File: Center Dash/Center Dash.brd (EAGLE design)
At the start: 159 x 86.7 mm, 73 parts, among them J1 502585-0470, U1 ADG3304BRUZ-REEL7, U2 TPS54540DDARQ1

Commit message: Worked on code
Updated board layouts since shit changed
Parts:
- added Q1, Q2, Q3, Q4: BSS138, FormE:BSS138
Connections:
- new net AMS_OUT: Q1.D, U$1.P$20
- new net BSPD_OUT: Q3.D, U$1.P$22
- new net IMD_OUT: Q2.D, U$1.P$21
- new net TPS_OUT: Q4.D, U$1.P$23
- net AMS: now also Q1.G; no longer U$1.P$20
- net BSPD: now also Q3.G; no longer U$1.P$22
- net GND: now also Q1.S, Q2.S, Q3.S, Q4.S
- net IMD: now also Q2.G; no longer U$1.P$21
- net TPS: now also Q4.G; no longer U$1.P$23
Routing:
- net AMS: track 40.5 -> 35.2 mm, vias 1 -> 2
- net TPS: track 35.7 -> 30.9 mm, vias 2 -> 3
- net IMD: track 35.5 -> 30.6 mm, vias 2 -> 3
- net BSPD: track 29.4 -> 24.6 mm, vias 0 -> 1
- net TPS_OUT: track 0.00 -> 2.93 mm
- net IMD_OUT: track 0.00 -> 2.83 mm
- net AMS_OUT: track 0.00 -> 2.80 mm
- net BSPD_OUT: track 0.00 -> 2.77 mm
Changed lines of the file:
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@@
 <attribute name="VALUE" x="19.812" y="24.511" size="1.27" layer="27"/>
+</element>
+<element name="Q1" library="FormE" package="BSS138" value="BSS138" x="1.905" y="61.976" smashed="yes" rot="MR0">
+<attribute name="NAME" x="4.445" y="59.436" size="1.27" layer="26" rot="MR90"/>
+</element>
+<element name="Q2" library="FormE" package="BSS138" value="BSS138" x="5.842" y="61.976" smashed="yes" rot="MR0">
+<attribute name="NAME" x="8.382" y="59.436" size="1.27" layer="26" rot="MR90"/>
+</element>
+<element name="Q3" library="FormE" package="BSS138" value="BSS138" x="10.033" y="61.976" smashed="yes" rot="MR0">
+<attribute name="NAME" x="12.573" y="59.436" size="1.27" layer="26" rot="MR90"/>
+</element>
+<element name="Q4" library="FormE" package="BSS138" value="BSS138" x="14.097" y="61.849" smashed="yes" rot="MR0">
+<attribute name="NAME" x="16.637" y="59.309" size="1.27" layer="26" rot="MR90"/>
 </element>
 </elements>
@@
 <wire x1="-30.876" y1="69.536" x2="-33.701" y2="69.536" width="0.3048" layer="16"/>
 <wire x1="-33.701" y1="69.536" x2="-33.906" y2="69.331" width="0.3048" layer="16"/>
+<contactref element="Q4" pad="S"/>
+<contactref element="Q3" pad="S"/>
+<contactref element="Q2" pad="S"/>
+<contactref element="Q1" pad="S"/>
 </signal>
 <signal name="+15V">
@@
 <signal name="AMS">
 <contactref element="U$2" pad="5"/>
-<contactref element="U$1" pad="P$20"/>
-<wire x1="2" y1="65.937" x2="2" y2="54.769" width="0.3048" layer="1"/>
-<wire x1="2" y1="54.769" x2="2.54" y2="54.229" width="0.3048" layer="1"/>
-<wire x1="2.54" y1="54.229" x2="2.54" y2="39.116" width="0.3048" layer="1"/>
+<wire x1="2.54" y1="39.116" x2="2.54" y2="54.229" width="0.3048" layer="1"/>
 <wire x1="2.54" y1="39.116" x2="2.921" y2="38.735" width="0.3048" layer="1"/>
 <via x="2.921" y="38.735" extent="1-16" drill="0.35"/>
@@
 <wire x1="14.224" y1="38.354" x2="14.224" y2="37.131" width="0.3048" layer="16"/>
 <wire x1="14.224" y1="37.131" x2="14.089" y2="36.996" width="0.3048" layer="16"/>
+<contactref element="Q1" pad="G"/>
+<wire x1="2.54" y1="54.229" x2="2.855" y2="54.544" width="0.3048" layer="1"/>
+<wire x1="2.855" y1="54.544" x2="2.855" y2="60.776" width="0.3048" layer="1"/>
+<via x="2.855" y="60.776" extent="1-16" drill="0.35"/>
 </signal>
 <signal name="IMD">
 <contactref element="U$2" pad="6"/>
-<contactref element="U$1" pad="P$21"/>
-<wire x1="6" y1="65.937" x2="6" y2="54.387" width="0.3048" layer="1"/>
-<wire x1="6" y1="54.387" x2="5.207" y2="53.594" width="0.3048" layer="1"/>
+<wire x1="6" y1="54.387" x2="5.9055" y2="54.2925" width="0.3048" layer="1"/>
+<wire x1="5.9055" y1="54.2925" x2="5.207" y2="53.594" width="0.3048" layer="1"/>
 <wire x1="5.207" y1="53.594" x2="5.207" y2="39.164" width="0.3048" layer="1"/>
 <wire x1="5.207" y1="39.164" x2="5.334" y2="39.037" width="0.3048" layer="1"/>
@@
 <wire x1="11.43" y1="39.037" x2="11.549" y2="38.918" width="0.3048" layer="1"/>
 <wire x1="11.549" y1="38.918" x2="11.549" y2="36.996" width="0.3048" layer="1"/>
+<contactref element="Q2" pad="G"/>
+<wire x1="6" y1="54.387" x2="6.792" y2="55.179" width="0.3048" layer="1"/>
+<wire x1="6.792" y1="55.179" x2="6.792" y2="60.776" width="0.3048" layer="1"/>
+<via x="6.792" y="60.776" extent="1-16" drill="0.35"/>
 </signal>
 <signal name="BSPD">
 <contactref element="U$2" pad="7"/>
-<contactref element="U$1" pad="P$22"/>
-<wire x1="10" y1="65.937" x2="10" y2="52.7177625" width="0.3048" layer="1"/>
-<wire x1="10" y1="52.7177625" x2="10.0504" y2="52.6673625" width="0.3048" layer="1"/>
-<wire x1="10.0504" y1="52.6673625" x2="10.0504" y2="38.0374" width="0.3048" layer="1"/>
+<wire x1="10.0504" y1="59.8434" x2="10.0504" y2="38.0374" width="0.3048" layer="1"/>
 <wire x1="10.0504" y1="38.0374" x2="9.009" y2="36.996" width="0.3048" layer="1"/>
+<contactref element="Q3" pad="G"/>
+<wire x1="10.0504" y1="59.8434" x2="10.983" y2="60.776" width="0.3048" layer="1"/>
+<via x="10.983" y="60.776" extent="1-16" drill="0.35"/>
 </signal>
 <signal name="TPS">
 <contactref element="U$2" pad="8"/>
-<contactref element="U$1" pad="P$23"/>
-<wire x1="14" y1="65.937" x2="14" y2="53.878" width="0.3048" layer="1"/>
-<wire x1="14" y1="53.878" x2="12.954" y2="52.832" width="0.3048" layer="1"/>
+<wire x1="14" y1="53.878" x2="13.716" y2="53.594" width="0.3048" layer="1"/>
+<wire x1="13.716" y1="53.594" x2="12.954" y2="52.832" width="0.3048" layer="1"/>
 <wire x1="12.954" y1="52.832" x2="12.954" y2="42.291" width="0.3048" layer="1"/>
 <wire x1="12.954" y1="42.291" x2="12.827" y2="42.164" width="0.3048" layer="1"/>
@@
 <wire x1="6.477" y1="42.037" x2="6.469" y2="42.029" width="0.3048" layer="1"/>
 <wire x1="6.469" y1="42.029" x2="6.469" y2="36.996" width="0.3048" layer="1"/>
+<contactref element="Q4" pad="G"/>
+<wire x1="14" y1="53.878" x2="15.047" y2="54.925" width="0.3048" layer="1"/>
+<wire x1="15.047" y1="54.925" x2="15.047" y2="60.649" width="0.3048" layer="1"/>
+<via x="15.047" y="60.649" extent="1-16" drill="0.35"/>
 </signal>
 <signal name="SW_BIT2">
@@
 <wire x1="50.165" y1="57.116" x2="50.165" y2="55.229" width="0.8128" layer="16"/>
 </signal>
+<signal name="AMS_OUT">
+<contactref element="Q1" pad="D"/>
+<contactref element="U$1" pad="P$20"/>
+<wire x1="1.905" y1="63.176" x2="1.905" y2="65.842" width="0.3048" layer="16"/>
+<wire x1="1.905" y1="65.842" x2="2" y2="65.937" width="0.3048" layer="16"/>
+</signal>
+<signal name="IMD_OUT">
+<contactref element="Q2" pad="D"/>
+<contactref element="U$1" pad="P$21"/>
+<wire x1="5.842" y1="63.176" x2="5.842" y2="65.779" width="0.3048" layer="16"/>
+<wire x1="5.842" y1="65.779" x2="6" y2="65.937" width="0.3048" layer="16"/>
+</signal>
+<signal name="BSPD_OUT">
+<contactref element="Q3" pad="D"/>
+<contactref element="U$1" pad="P$22"/>
+<wire x1="10.033" y1="63.176" x2="10.033" y2="65.904" width="0.3048" layer="16"/>
+<wire x1="10.033" y1="65.904" x2="10" y2="65.937" width="0.3048" layer="16"/>
+</signal>
+<signal name="TPS_OUT">
+<contactref element="Q4" pad="D"/>
+<contactref element="U$1" pad="P$23"/>
+<wire x1="14.097" y1="63.049" x2="14.097" y2="65.84" width="0.3048" layer="16"/>
+<wire x1="14.097" y1="65.84" x2="14" y2="65.937" width="0.3048" layer="16"/>
+</signal>
 </signals>

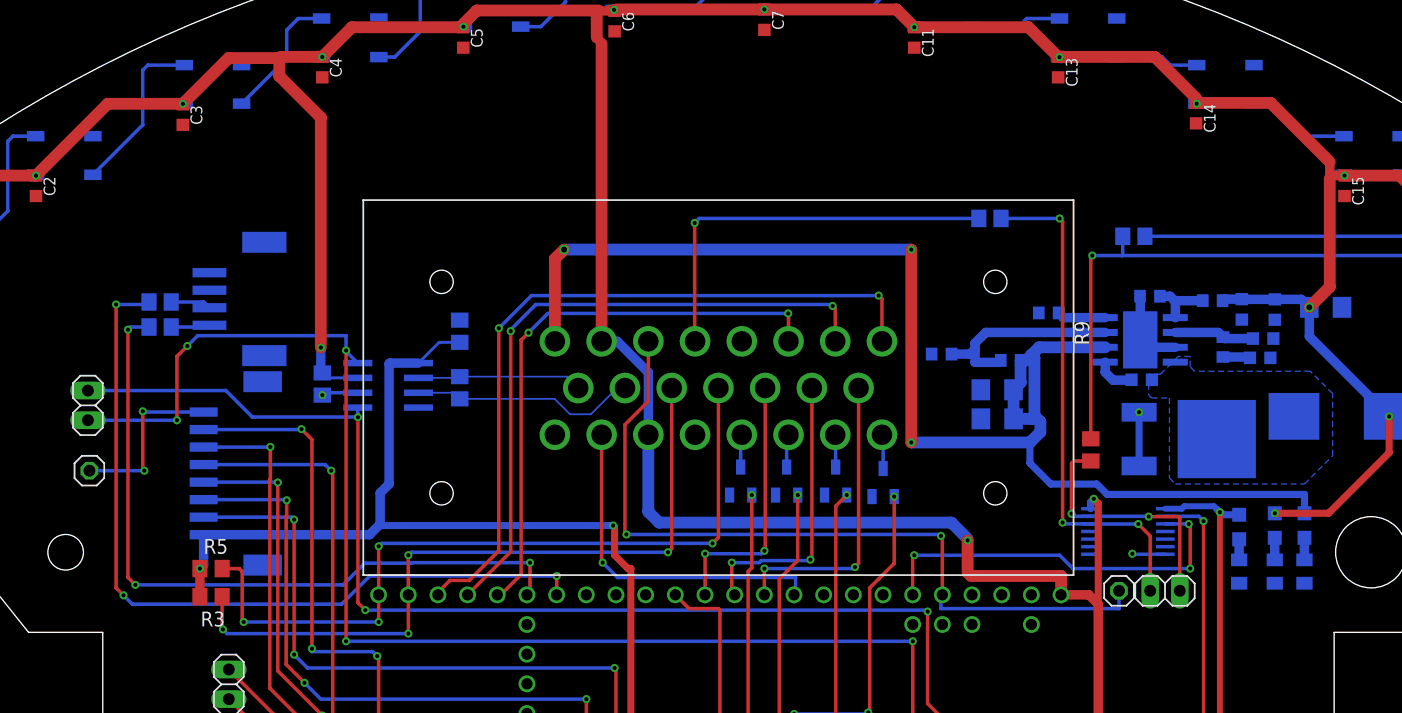
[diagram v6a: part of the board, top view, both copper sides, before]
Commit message: Fix for daqbus CAN
Added another can transceiver for the daq bus
Moved the ignition1 and 2 to different pins to account for the teensy can bus lines
Fixed the can code from flexcan
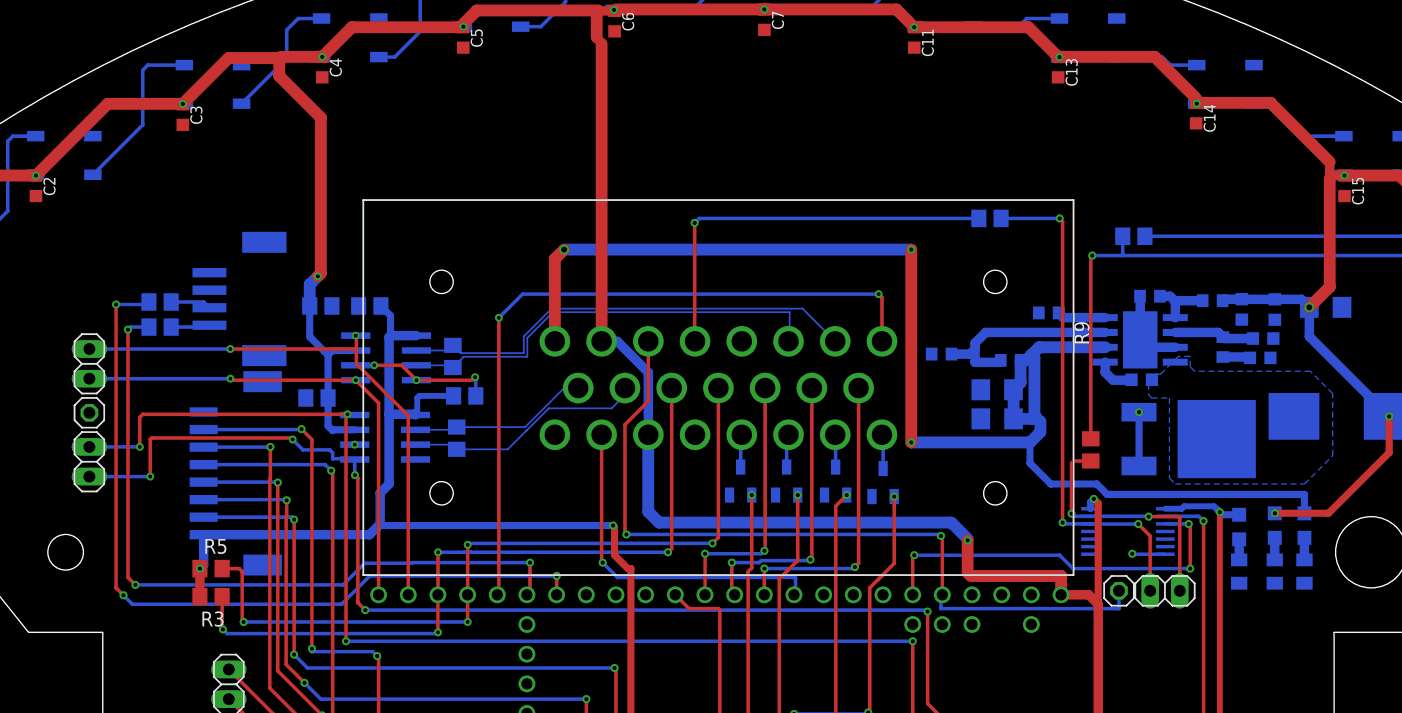
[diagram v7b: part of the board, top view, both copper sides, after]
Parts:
- added C17, C21: .1uF, rcl:C0805
- added JP9: (no value), pinhead:1X02
- added R16: 120, rcl:R0805
- added U4: (no value), FormE:SOIC8-N_MC
- moved C20 5.55 mm to (-21.7, 69.3), turned to 180 degrees
- moved JP4 4.95 mm to (-53.8, 67.8)
- moved JP6 4.83 mm to (-53.8, 63.6), turned to 270 degrees
- moved U3 4.45 mm to (-28.5, 65.7)
- moved R4 4.33 mm to (-22.4, 65.6)
- moved C19 1.28 mm to (-34.4, 69.1), turned to 0 degrees
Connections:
- net CAN_N renamed CARCAN_N
- net CAN_P renamed CARCAN_P
- net CAN_RX renamed CARCAN_RX
- net CAN_TX renamed CARCAN_TX
- removed net SPARE_2: U$1.P$7, U$2.36/A17
- removed net SPARE_3: U$1.P$6, U$2.37/A18
- new net DAQCAN_N: R16.2, U$1.P$7, U4.6
- new net DAQCAN_P: R16.1, U$1.P$6, U4.7
- new net DAQCAN_RX: JP9.2, U$2.34/A15, U4.4
- new net DAQCAN_TX: JP9.1, U$2.33/A14, U4.1
- net +3V3: now also C21.1, U4.5
- net +5V: now also C17.1, U4.3
- net GND: now also C17.2, C21.2, U4.2, U4.8
- net IGNITION_1: now also R3.2, U$1.P$11, U$2.35/A16; no longer R5.2, U$1.P$12, U$2.33/A14
- net IGNITION_2: now also R5.2, U$1.P$12, U$2.36/A17; no longer R3.2, U$1.P$11, U$2.34/A15
- net SPARE_1: now also U$2.37/A18; no longer U$2.35/A16
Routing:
- net SPARE_2: track 55.8 -> 0.00 mm, vias 2 -> 0
- net SPARE_3: track 49.0 -> 0.00 mm, vias 2 -> 0
- net DAQCAN_RX: track 0.00 -> 46.9 mm, vias 0 -> 2
- net DAQCAN_TX: track 0.00 -> 42.0 mm, vias 0 -> 2
- net DAQCAN_N: track 0.00 -> 39.9 mm
- net DAQCAN_P: track 0.00 -> 37.5 mm
- net CARCAN_RX: track 115.7 -> 104.8 mm, vias 5 -> 4
- net +3V3: track 172.4 -> 180.1 mm
- net +5V: track 384.4 -> 391.7 mm
- net GND: track 32.8 -> 27.0 mm, vias 5 -> 6
- net IGNITION_2: track 62.1 -> 66.5 mm
- net IGNITION_1: track 66.4 -> 62.2 mm
- net SPARE_1: track 63.6 -> 61.3 mm
- net CARCAN_TX: track 104.2 -> 102.8 mm, vias 3 -> 5
- net CARCAN_N: track 14.1 -> 15.4 mm
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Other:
- board text added: "CARCAN_RX"
- board text added: "CARCAN_TX"
- board text removed: "CAN_RX"
- board text removed: "CAN_TX"
